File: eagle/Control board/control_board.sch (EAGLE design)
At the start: 54 parts

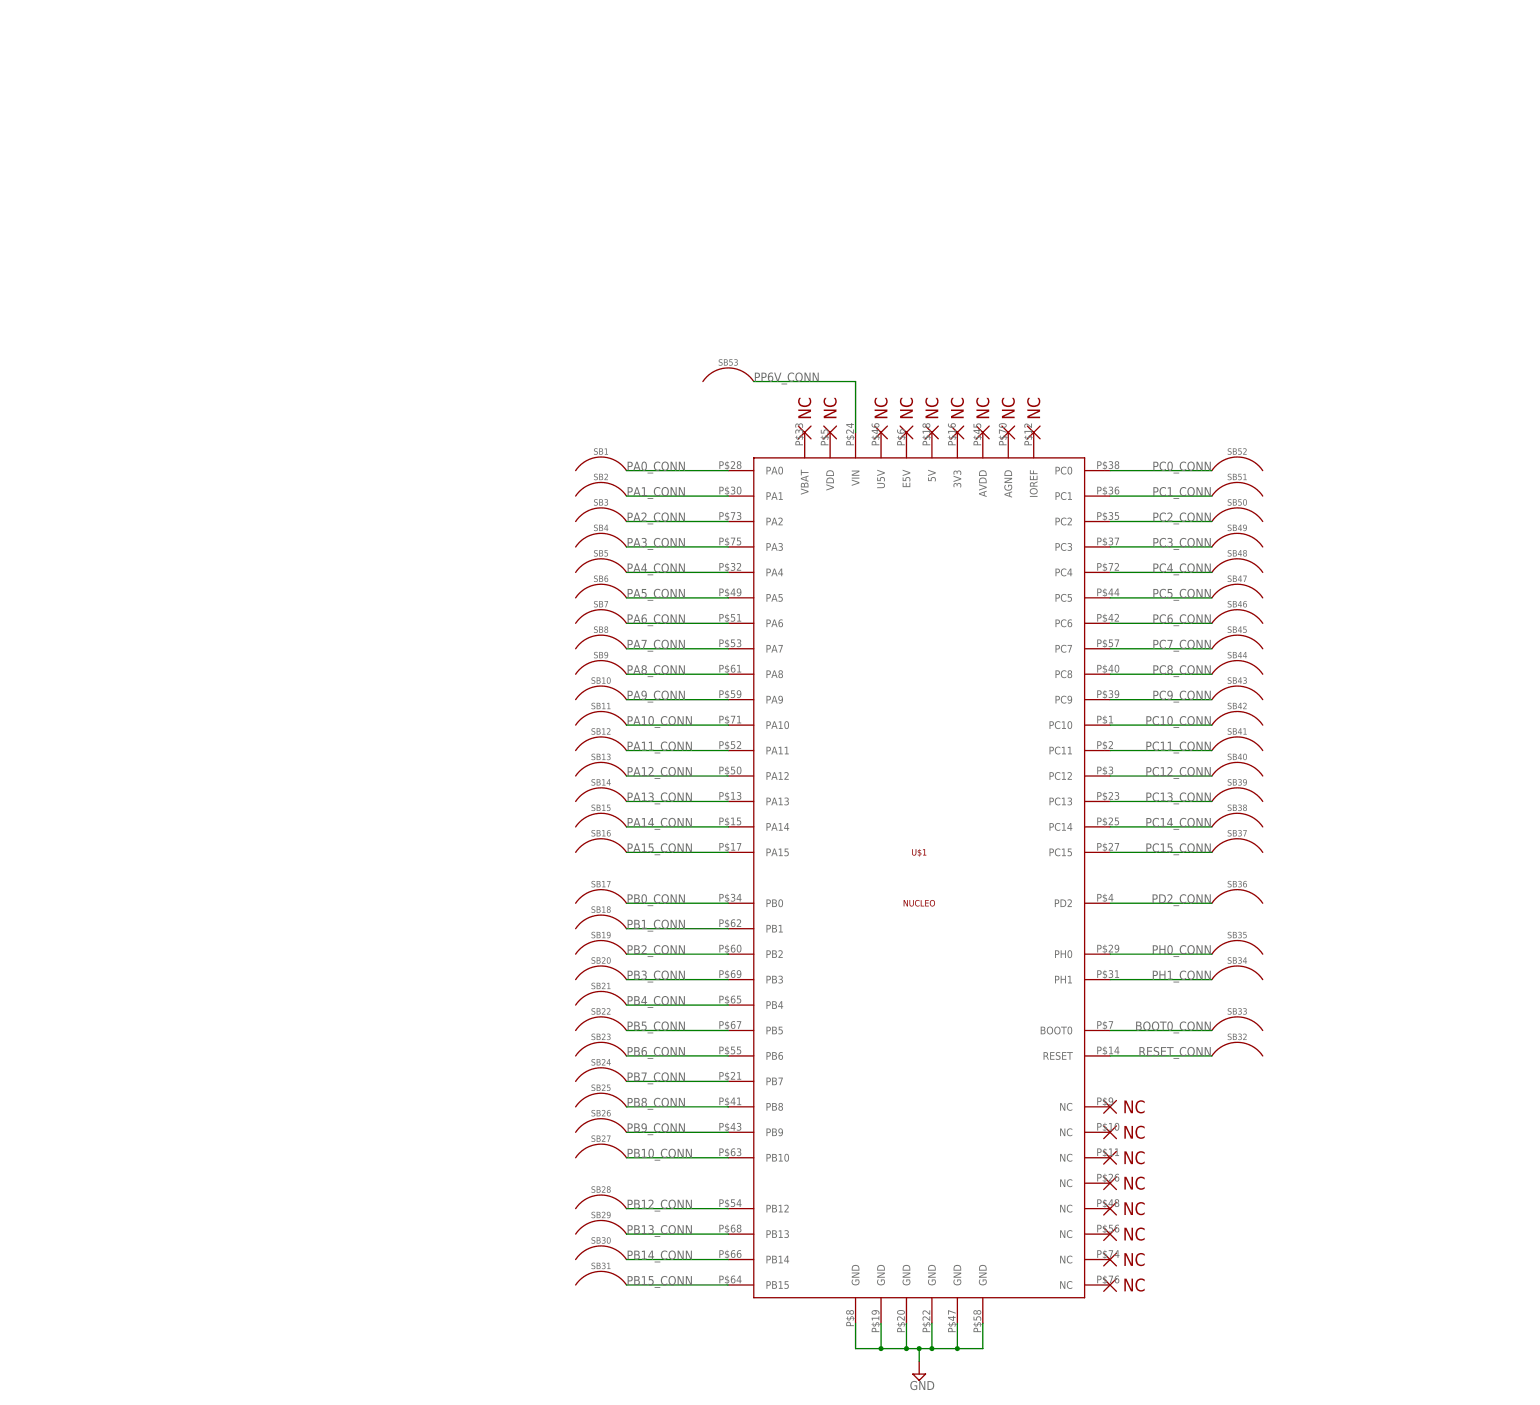
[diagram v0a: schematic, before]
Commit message: Added battery and regulators. Added silks to nucleo footprint.
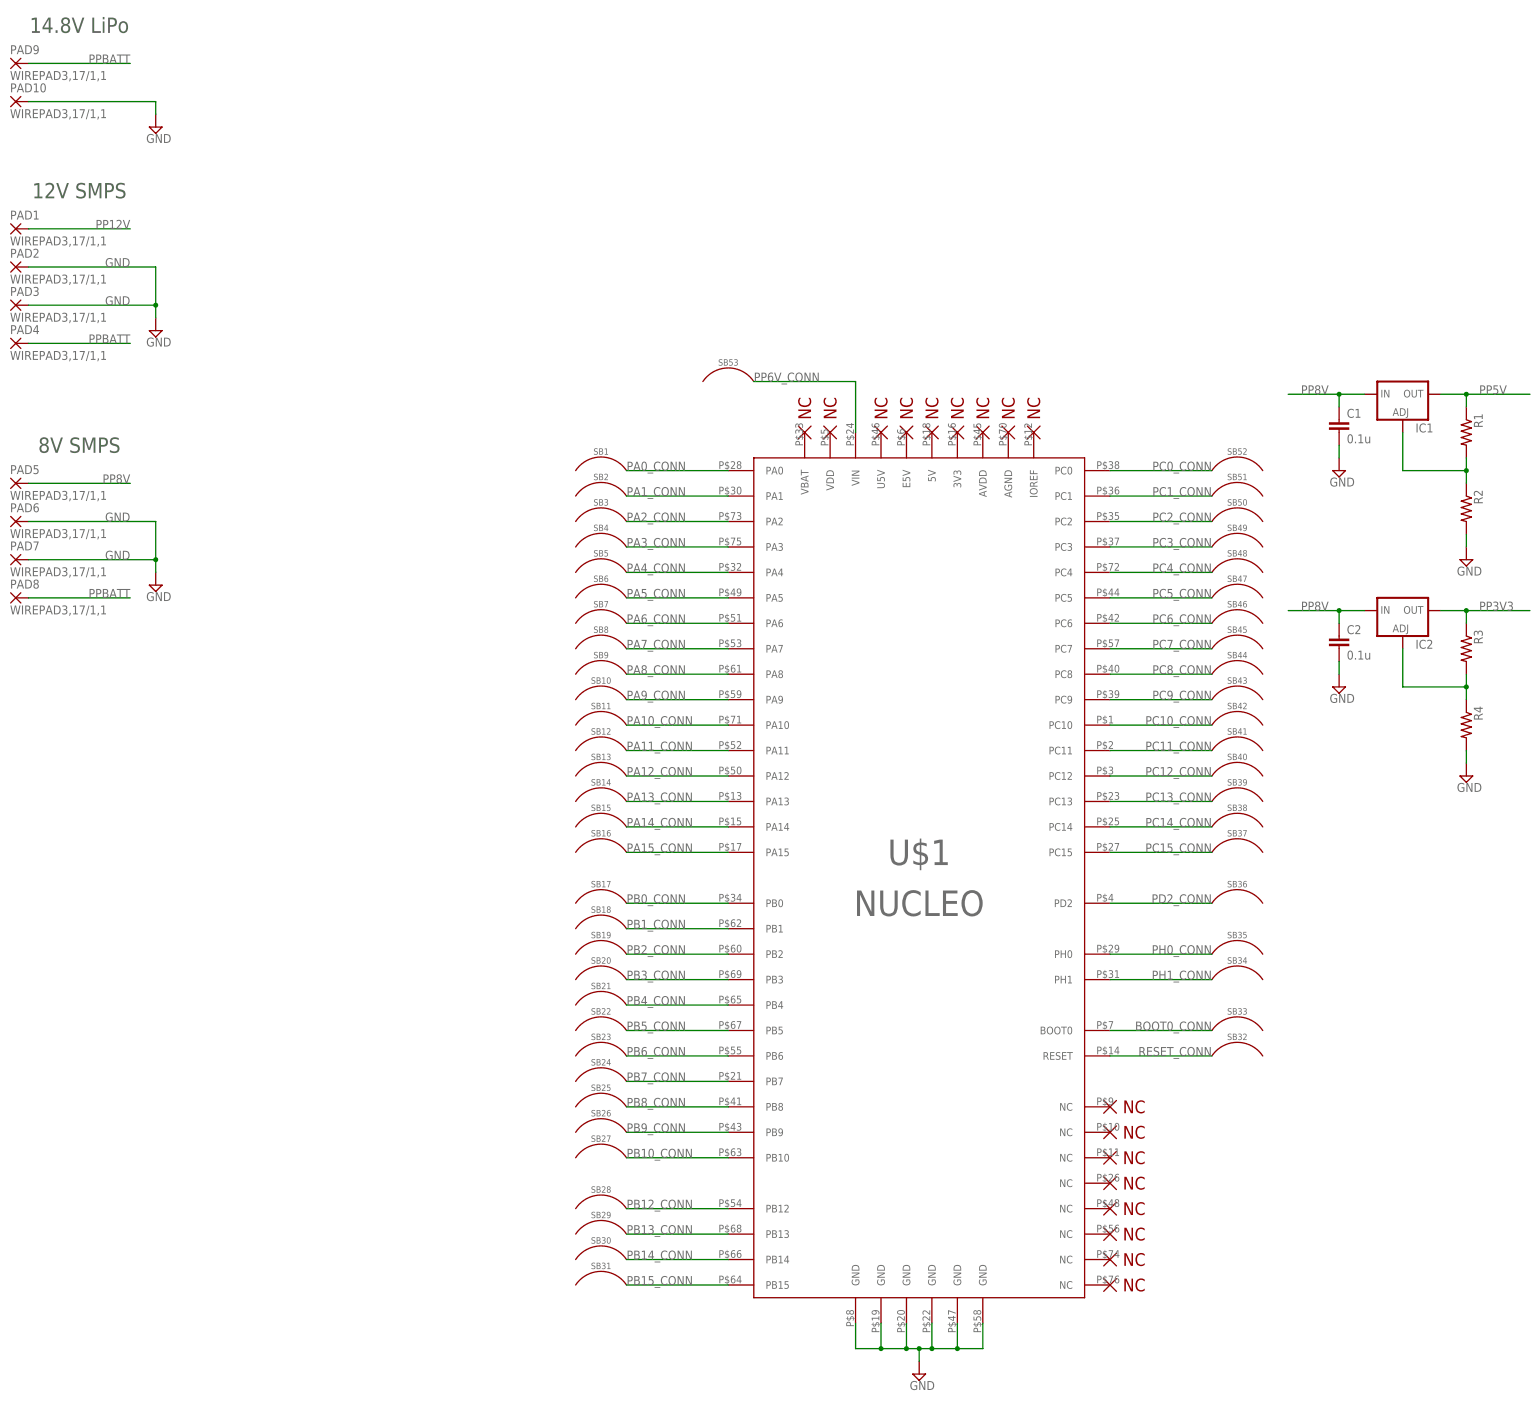
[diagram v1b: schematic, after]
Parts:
- added C1, C2: 0.1u, rcl:C-EUC0603
- added IC1, IC2: (no value), custom:LM317TS
- added PAD1, PAD10, PAD2, PAD3, PAD4, PAD5, PAD6, PAD7, PAD8, PAD9: WIREPAD3,17/1,1, wirepad:WIREPAD3,17/1,1
- added R1, R2, R3, R4: (no value), rcl:R-US_R0603
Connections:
- new net N$1: IC2.ADJ, R3.2, R4.1
- new net N$3: IC1.ADJ, R1.2, R2.1
- new net PP12V: PAD1.P
- new net PP3V3: IC2.OUT, R3.1
- new net PP5V: IC1.OUT, R1.1
- new net PP8V: C1.1, C2.1, IC1.IN, IC2.IN, PAD5.P
- new net PPBATT: PAD4.P, PAD8.P, PAD9.P
- net GND: now also C1.2, C2.2, PAD10.P, PAD2.P, PAD3.P, PAD6.P, PAD7.P, R2.2, R4.2
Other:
- note added: "12V SMPS"
- note added: "14.8V LiPo"
- note added: "8V SMPS"

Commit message: Added connectors, more layout stuff
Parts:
- added C3, C4: 0.1uF, rcl:C-EUC0603
- added R5, R6: 1k, rcl:R-US_R0603
- added SB54, SB55, SB56, SB57, SB58, SB59, SB60, SB61, SB62, SB63, SB64, SB65, SB66, SB67, SB68, SB69, SB70, SB71, SB72, SB73, SB74, SB75, SB76, SB77, SB78, SB79, SB80, SB81, SB82, SB83, SB84, SB85, SB86, SB87, SB88, SB89, SB90, SB91, SB92, SB93: SOLDER_BRIDGE, custom:SOLDER_BRIDGE
- added X1, X12: JST-XH-02-PIN-LONG-PAD, con-jst-xh:JST-XH-02-PIN-LONG-PAD
- added X10, X11, X9: JST-XH-07-PIN-LONG-PAD, con-jst-xh:JST-XH-07-PIN-LONG-PAD
- added X2, X3, X4, X5, X6, X7: JST-XH-06-PIN-LONG-PAD, con-jst-xh:JST-XH-06-PIN-LONG-PAD
- added X8: JST-XH-04-PIN-LONG-PAD, con-jst-xh:JST-XH-04-PIN-LONG-PAD
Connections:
- net PP6V_CONN renamed PP8V_CONN
- new net IMU_SCL: SB64.P$2, X8-2.S
- new net IMU_SDA: SB69.P$2, X8-3.S
- new net IMU_VCC: SB59.P$2, X8-1.S
- new net M1_1: SB85.P$1
- new net M1_2: SB86.P$1
- new net M1_3: SB87.P$1
- new net M1_4: SB88.P$1
- new net M2_1: SB74.P$1
- new net M2_2: SB79.P$1
- new net M2_3: SB84.P$1
- new net M2_4: SB89.P$1
- new net M3_1: SB90.P$1
- new net M3_2: SB91.P$1
- new net M3_3: SB92.P$1
- new net M3_4: SB93.P$1
- new net MOTOR1_1EN: SB85.P$2, X9-4.S
- new net MOTOR1_2EN: SB86.P$2, X9-5.S
- new net MOTOR1_3EN: SB87.P$2, X9-6.S
- new net MOTOR1_4EN: SB88.P$2, X9-7.S
- new net MOTOR2_1EN: SB74.P$2, X10-4.S
- new net MOTOR2_2EN: SB79.P$2, X10-5.S
- new net MOTOR2_3EN: SB84.P$2, X10-6.S
- new net MOTOR2_4EN: SB89.P$2, X10-7.S
- new net MOTOR3_1EN: SB90.P$2, X11-4.S
- new net MOTOR3_2EN: SB91.P$2, X11-5.S
- new net MOTOR3_3EN: SB92.P$2, X11-6.S
- new net MOTOR3_4EN: SB93.P$2, X11-7.S
- new net RF1_G: SB57.P$1
- new net RF1_GPIO: SB57.P$2, X2-5.S
- new net RF1_SCL: SB55.P$2, X2-3.S
- new net RF1_SDA: SB56.P$2, X2-4.S
- new net RF1_X: SB58.P$1
- new net RF1_XSHUT: SB58.P$2, X2-6.S
- new net RF2_G: SB62.P$1
- new net RF2_GPIO: SB62.P$2, X3-5.S
- new net RF2_SCL: SB60.P$2, X3-3.S
- new net RF2_SDA: SB61.P$2, X3-4.S
- new net RF2_X: SB63.P$1
- new net RF2_XSHUT: SB63.P$2, X3-6.S
- new net RF3_G: SB67.P$1
- new net RF3_GPIO: SB67.P$2, X4-5.S
- new net RF3_SCL: SB65.P$2, X4-3.S
- new net RF3_SDA: SB66.P$2, X4-4.S
- new net RF3_X: SB68.P$1
- new net RF3_XSHUT: SB68.P$2, X4-6.S
- new net RF4_G: SB72.P$1
- new net RF4_GPIO: SB72.P$2, X5-5.S
- new net RF4_SCL: SB70.P$2, X5-3.S
- new net RF4_SDA: SB71.P$2, X5-4.S
- new net RF4_X: SB73.P$1
- new net RF4_XSHUT: SB73.P$2, X5-6.S
- new net RF5_G: SB77.P$1
- new net RF5_GPIO: SB77.P$2, X6-5.S
- new net RF5_SCL: SB75.P$2, X6-3.S
- new net RF5_SDA: SB76.P$2, X6-4.S
- new net RF5_X: SB78.P$1
- new net RF5_XSHUT: SB78.P$2, X6-6.S
- new net RF6_G: SB82.P$1
- new net RF6_GPIO: SB82.P$2, X7-5.S
- new net RF6_SCL: SB80.P$2, X7-3.S
- new net RF6_SDA: SB81.P$2, X7-4.S
- new net RF6_X: SB83.P$1
- new net RF6_XSHUT: SB83.P$2, X7-6.S
- new net RF_VCC: SB54.P$2, X2-1.S, X3-1.S, X4-1.S, X5-1.S, X6-1.S, X7-1.S
- new net SCL: SB55.P$1, SB60.P$1, SB64.P$1, SB65.P$1, SB70.P$1, SB75.P$1, SB80.P$1
- new net SDA: SB56.P$1, SB61.P$1, SB66.P$1, SB69.P$1, SB71.P$1, SB76.P$1, SB81.P$1
- new net SW1: C3.2, C4.2, R5.1, R6.1, X1-1.S, X12-1.S
- net GND: now also C3.1, C4.1, X1-2.S, X10-2.S, X11-2.S, X12-2.S, X2-2.S, X3-2.S, X4-2.S, X5-2.S, X6-2.S, X7-2.S, X8-4.S, X9-2.S
- net PC0_CONN: now also SB52.P$2; no longer SB52.P$1
- net PC1_CONN: now also SB51.P$2; no longer SB51.P$1
- net PC7_CONN: now also SB45.P$2; no longer SB45.P$1
- net PC9_CONN: now also SB43.P$2; no longer SB43.P$1
- net PP12V: now also X10-1.S, X11-1.S, X9-1.S
- net PP3V3: now also R5.2, R6.2, SB54.P$1, SB59.P$1
- net PP5V: now also X10-3.S, X11-3.S, X9-3.S
- net PP8V: now also SB53.P$1
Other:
- note added: "7V SMPS"
- note added: "IMU"
- note added: "MOTOR DRIVERS"
- note added: "Microswitches"
- note added: "VL53L0X Rangefinders"
- note removed: "8V SMPS"

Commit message: Added more stuff
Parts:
- added LED1: (no value), adafruit:LEDCHIPLED_0805
- added R7: 1k, rcl:R-US_R0603
- added SB100, SB101, SB102, SB103, SB104, SB105, SB106, SB108, SB109, SB110, SB111, SB112, SB113, SB114, SB115, SB94, SB95, SB96, SB97, SB98, SB99: SOLDER_BRIDGE, custom:SOLDER_BRIDGE
- added SW1: SPST_TACT-EVQQ2, adafruit:SPST_TACT-EVQQ2
- added X13, X14: JST-XH-03-PIN-LONG-PAD, con-jst-xh:JST-XH-03-PIN-LONG-PAD
- added X15, X17: JST-XH-08-PIN-LONG-PAD, con-jst-xh:JST-XH-08-PIN-LONG-PAD
- added X16, X18: JST-XH-02-PIN-LONG-PAD, con-jst-xh:JST-XH-02-PIN-LONG-PAD
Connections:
- net PA13_CONN renamed TMS
- net PA14_CONN renamed TCK
- net PA2_CONN renamed USART2_TX
- net PA3_CONN renamed USART2_RX
- net PA5_CONN renamed BRD_LED
- net PB3_CONN renamed SWO
- net PC13_CONN renamed BRD_BUTTN
- net PP8V renamed PP7V
- new net IR1_1: SB5.P$1, SB99.P$1
- new net IR1_2: SB100.P$1, SB11.P$1
- new net IR1_3: SB101.P$1, SB12.P$1
- new net IR1_4: SB102.P$1, SB17.P$1
- new net IR1_5: SB103.P$1, SB18.P$1
- new net IR1_6: SB104.P$1, SB19.P$1
- new net IR1_7: SB105.P$1, SB21.P$1
- new net IR1_8: SB106.P$1, SB22.P$1
- new net IR1_IN1: SB99.P$2, X15-1.S
- new net IR1_IN2: SB100.P$2, X15-2.S
- new net IR1_IN3: SB101.P$2, X15-3.S
- new net IR1_IN4: SB102.P$2, X15-4.S
- new net IR1_IN5: SB103.P$2, X15-5.S
- new net IR1_IN6: SB104.P$2, X15-6.S
- new net IR1_IN7: SB105.P$2, X15-7.S
- new net IR1_IN8: SB106.P$2, X15-8.S
- new net IR2_1: SB108.P$1, SB28.P$1
- new net IR2_2: SB109.P$1, SB29.P$1
- new net IR2_3: SB110.P$1, SB30.P$1
- new net IR2_4: SB111.P$1, SB31.P$1
- new net IR2_5: SB112.P$1, SB52.P$1
- new net IR2_6: SB113.P$1, SB51.P$1
- new net IR2_7: SB114.P$1, SB50.P$2
- new net IR2_8: SB115.P$1, SB48.P$2
- new net IR2_IN1: SB108.P$2, X17-1.S
- new net IR2_IN2: SB109.P$2, X17-2.S
- new net IR2_IN3: SB110.P$2, X17-3.S
- new net IR2_IN4: SB111.P$2, X17-4.S
- new net IR2_IN5: SB112.P$2, X17-5.S
- new net IR2_IN6: SB113.P$2, X17-6.S
- new net IR2_IN7: SB114.P$2, X17-7.S
- new net IR2_IN8: SB115.P$2, X17-8.S
- new net IR_VCC: SB98.P$2, X16-1.S, X18-1.S
- new net N$2: SB7.P$1
- new net N$43: SB42.P$2
- new net N$44: SB41.P$2
- new net N$49: SB36.P$2
- new net N$50: SB35.P$2
- new net N$51: SB34.P$2
- new net RESET_BTN: SB32.P$2, SW1.P, SW1.P1
- new net SERVO1: SB1.P$1, SB95.P$1
- new net SERVO1_PWM: SB95.P$2, X13-2.S
- new net SERVO1_VCC: SB94.P$2, X13-1.S
- new net SERVO2: SB2.P$1, SB97.P$1
- new net SERVO2_PWM: SB97.P$2, X14-2.S
- new net SERVO2_VCC: SB96.P$2, X14-1.S
- new net SW2: C4.2, R6.1, X12-1.S
- net GND: now also SW1.S, SW1.S1, X13-3.S, X14-3.S, X16-2.S, X18-2.S
- net M1_1: now also SB23.P$1
- net M1_2: now also SB13.P$1
- net M1_3: now also SB26.P$1
- net M1_4: now also SB47.P$2
- net M2_1: now also SB24.P$1
- net M2_2: now also SB9.P$1
- net M2_3: now also SB25.P$1
- net M2_4: now also SB10.P$1
- net M3_1: now also SB46.P$2
- net M3_2: now also SB45.P$1
- net M3_3: now also SB44.P$2
- net M3_4: now also SB43.P$1
- net PP3V3: now also SB98.P$1
- net PP5V: now also SB94.P$1, SB96.P$1
- net RF1_G: now also SB8.P$1
- net RF2_G: now also SB49.P$2
- net SCL: now also SB27.P$1
- net SDA: now also SB40.P$2
- net SW1: no longer C4.2, R6.1, X12-1.S
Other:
- note added: "IR PROXIMITY"
- note added: "SERVOS"
- moved on the sheet: C3, C4, R5, R6, SB59, SB64, SB69, SB74, SB79, SB84, SB85, SB86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

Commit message: Added cube, gpio expander, rearranged gpios
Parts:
- added C5, C6, C7: 0.1uF, rcl:C-EUC0603
- added LED2, LED3, LED4: (no value), adafruit:LEDCHIPLED_0805
- added R10, R8, R9: 82, rcl:R-US_R0603
- added R11, R12: 100, rcl:R-US_R0603
- added SB107, SB116, SB117, SB118, SB119, SB120: SOLDER_BRIDGE, custom:SOLDER_BRIDGE
- added SW2: SPST_TACT-EVQQ2, adafruit:SPST_TACT-EVQQ2
- added U1, U5, U6: TCA9554A, custom:TCA9554A
- LED1: DIGI (none) -> 732-4971-1-ND
- R5, R6: value 1k -> 4.7k
- R7: value 1k -> 430
- SW1: DIGI (none) -> P12955SCT-ND
- U2, U3: value (none) -> LM317
- U4: value NUCLEO -> STM32F446
- renumbered IC1 to U2, IC2 to U3, U$1 to U4
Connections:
- net PC14_CONN renamed OSC32_IN
- net PC15_CONN renamed OSC32_OUT
- net PH0_CONN renamed OSC_IN
- net PH1_CONN renamed OSC_OUT
- removed net N$2: SB7.P$1
- removed net N$44: SB41.P$2
- removed net N$49: SB36.P$2
- removed net N$50: SB35.P$2
- removed net N$51: SB34.P$2
- removed net SCL: SB27.P$1, SB55.P$1, SB60.P$1, SB64.P$1, SB65.P$1, SB70.P$1, SB75.P$1, SB80.P$1
- removed net SDA: SB40.P$2, SB56.P$1, SB61.P$1, SB66.P$1, SB69.P$1, SB71.P$1, SB76.P$1, SB81.P$1
- new net DBG_BUTTON: SB39.P$2, SW2.P, SW2.P1
- new net GPIOEXP1_SCL: SB116.P$2, U1.SCL
- new net GPIOEXP1_SDA: SB107.P$2, U1.SDA
- new net GPIOEXP2_SCL: SB118.P$2, U5.SCL
- new net GPIOEXP2_SDA: SB117.P$2, U5.SDA
- new net GPIOEXP3_P6: R9.1, U6.P6
- new net GPIOEXP3_P7: R10.1, U6.P7
- new net GPIOEXP3_SCL: SB120.P$2, U6.SCL
- new net GPIOEXP3_SDA: SB119.P$2, U6.SDA
- new net I2C2_SCL: SB116.P$1, SB118.P$1, SB120.P$1, SB27.P$1, SB55.P$1, SB60.P$1, SB64.P$1, SB65.P$1, SB70.P$1, SB75.P$1, SB80.P$1
- new net I2C2_SDA: SB107.P$1, SB117.P$1, SB119.P$1, SB40.P$2, SB56.P$1, SB61.P$1, SB66.P$1, SB69.P$1, SB71.P$1, SB76.P$1, SB81.P$1
- new net I2C3_SCL: SB9.P$1
- new net I2C3_SDA: SB21.P$1
- new net LED_3V3: LED2.A, R8.2
- new net LED_5V: LED1.A, R7.2
- new net LED_GPIOEXP3_P6: LED3.A, R9.2
- new net LED_GPIOEXP3_P7: LED4.A, R10.2
- new net N$4: SB43.P$1
- new net SW1_ILIM: C3.1, R11.2
- new net SW2_ILIM: C4.1, R12.2
- net GND: now also C5.1, C6.1, C7.1, LED1.C, LED2.C, LED3.C, LED4.C, R11.1, R12.1, SW2.S, SW2.S1, U1.A0, U1.A1, U1.A2, U1.GND, U5.A1, U5.A2, U5.GND, U6.A0, U6.A2, U6.GND; no longer C3.1, C4.1
- net IR1_1: now also U1.P0; no longer SB5.P$1
- net IR1_2: now also U1.P1; no longer SB11.P$1
- net IR1_3: now also U1.P2; no longer SB12.P$1
- net IR1_4: now also U1.P3; no longer SB17.P$1
- net IR1_5: now also U1.P4; no longer SB18.P$1
- net IR1_6: now also U1.P5; no longer SB19.P$1
- net IR1_7: now also U1.P6; no longer SB21.P$1
- net IR1_8: now also U1.P7; no longer SB22.P$1
- net IR2_1: now also U5.P0; no longer SB28.P$1
- net IR2_2: now also U5.P1; no longer SB29.P$1
- net IR2_3: now also U5.P2; no longer SB30.P$1
- net IR2_4: now also U5.P3; no longer SB31.P$1
- net IR2_5: now also U5.P4; no longer SB52.P$1
- net IR2_6: now also U5.P5; no longer SB51.P$1
- net IR2_7: now also U5.P6; no longer SB50.P$2
- net IR2_8: now also U5.P7; no longer SB48.P$2
- net M1_2: no longer SB13.P$1
- net M1_3: now also SB24.P$1; no longer SB26.P$1
- net M1_4: no longer SB47.P$2
- net M2_1: now also SB25.P$1; no longer SB24.P$1
- net M2_2: now also SB11.P$1; no longer SB9.P$1
- net M2_3: now also SB26.P$1; no longer SB25.P$1
- net M2_4: now also SB22.P$1; no longer SB10.P$1
- net M3_1: now also SB7.P$1
- net M3_2: now also SB48.P$2; no longer SB45.P$1
- net M3_3: now also SB8.P$1
- net M3_4: now also SB29.P$1; no longer SB43.P$1
- net PP3V3: now also C5.2, C6.2, C7.2, R8.1, U1.VCC, U5.A0, U5.VCC, U6.A1, U6.VCC
- net PP5V: now also R7.1
- net RF1_G: now also SB52.P$1; no longer SB8.P$1
- net RF1_X: now also U6.P0
- net RF2_G: now also SB51.P$1; no longer SB49.P$2
- net RF2_X: now also U6.P1
- net RF3_G: now also SB17.P$1
- net RF3_X: now also U6.P2
- net RF4_G: now also SB1.P$1
- net RF4_X: now also U6.P3
- net RF5_G: now also SB36.P$2
- net RF5_X: now also U6.P4
- net RF6_G: now also SB41.P$2
- net RF6_X: now also U6.P5
- net SERVO1: now also SB30.P$1; no longer SB1.P$1
- net SERVO2: now also SB31.P$1; no longer SB2.P$1
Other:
- note added: "0x52 0x53 0x54 0x55 0x56 0x57 0x58 0x69 0x19 0x1E 0x38 0x39 0x3A"
- note added: "GPIO EXPANDERS"
- note added: "I2C ADDRESS TABLE"
- note added: "POWER"
- note added: "RF Initial RF1 RF2 RF3 RF4 RF5 RF6 IMU_GYRO IMU_ACCEL IMU_MAG GPIO_EXPANDER1 GPIO_EXPANDER2 GPIO_EXPANDER3"
- note added: "SENSOR CONNECTORS"
- note added: "STM32F446 NUCLEO"
- note added: "Vf=2.9V@5mA"
